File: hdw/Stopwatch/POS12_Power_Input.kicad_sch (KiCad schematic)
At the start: 17 parts

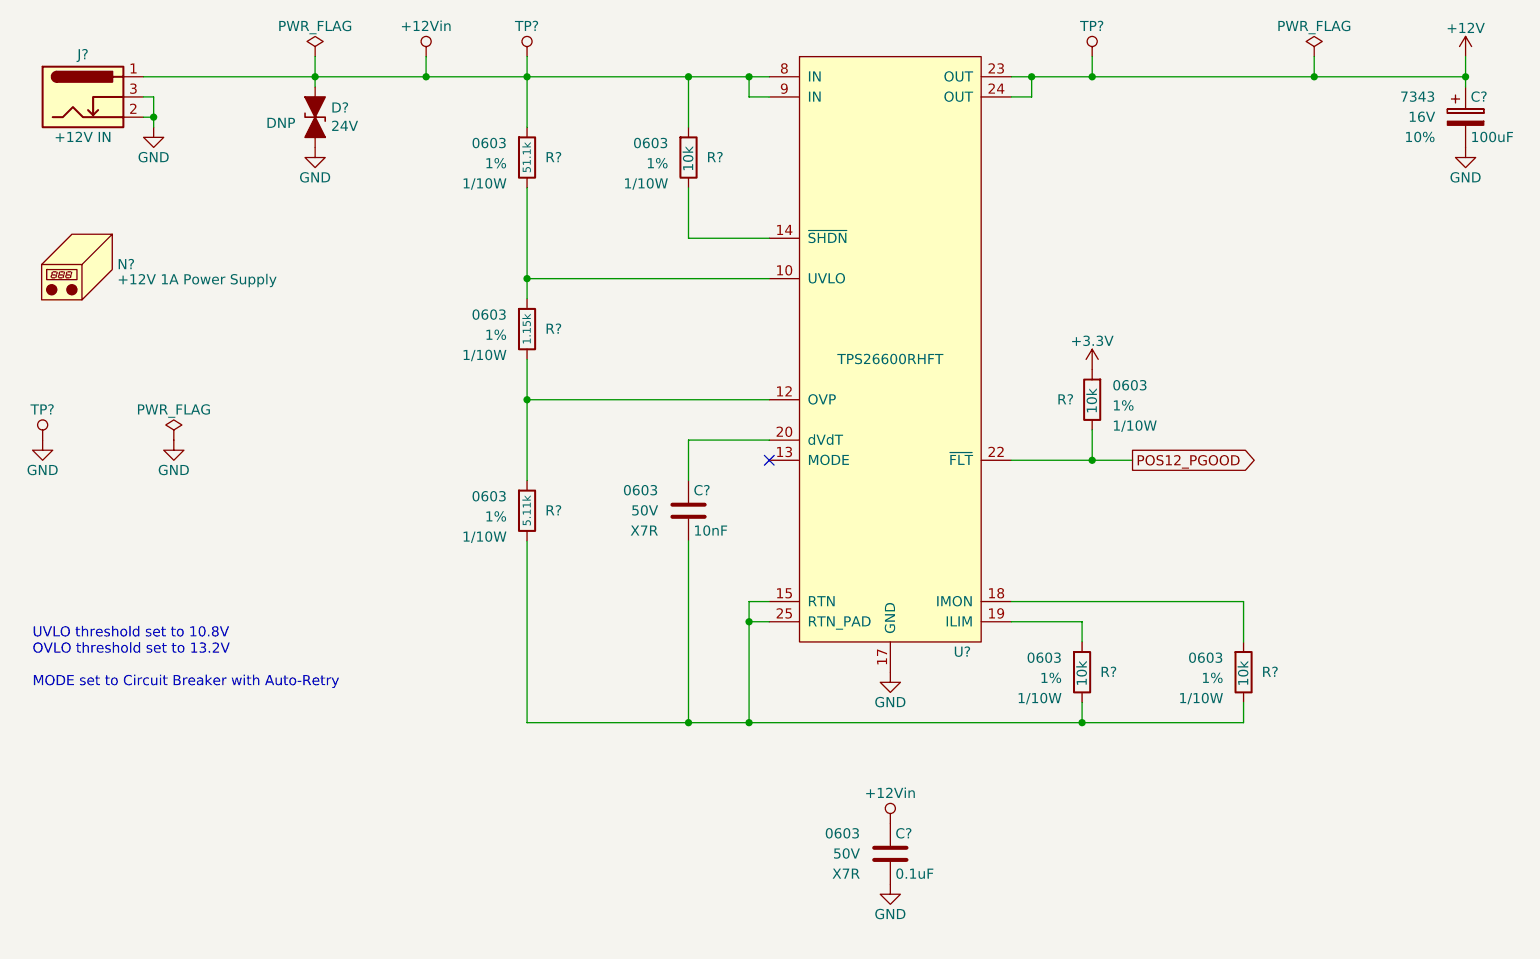
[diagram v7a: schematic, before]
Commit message: Assigned some digikey pns
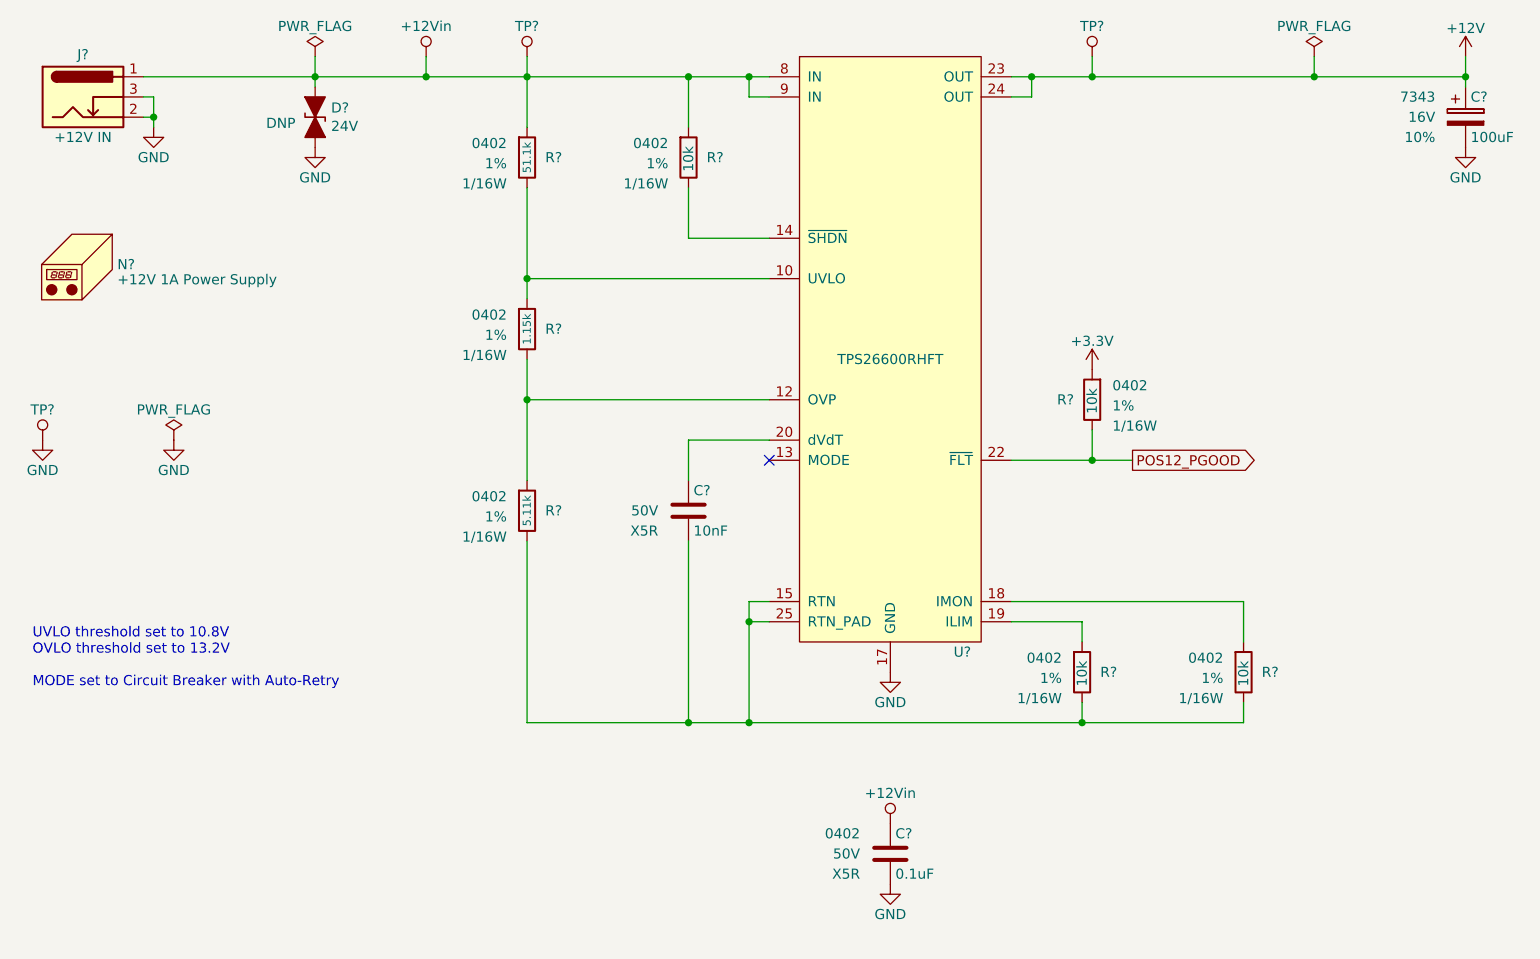
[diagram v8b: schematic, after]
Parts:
- C?: footprint Capacitors_SMD:C_0603 -> Capacitors_SMD:C_0402; Dielectric X7R -> X5R; Digi-Key PN 311-1344-1-ND -> 490-10697-1-ND; display_footprint 0603 -> 0402
- C?: footprint Capacitors_SMD:C_0603 -> Capacitors_SMD:C_0402; Dielectric X7R -> X5R; Digi-Key PN 1276-1921-1-ND -> 445-12201-1-ND; display_footprint 0603 -> (none)
- R? (x4): footprint Resistors_SMD:R_0603 -> Resistors_SMD:R_0402; Digi-Key PN RMCF0603FT10K0CT-ND -> RMCF0402FT10K0CT-ND; Wattage 1/10W -> 1/16W; display_footprint 0603 -> 0402
- R?: footprint Resistors_SMD:R_0603 -> Resistors_SMD:R_0402; Digi-Key PN RMCF0603FT10K0CT-ND -> RMCF0402FT1K15CT-ND; Wattage 1/10W -> 1/16W; display_footprint 0603 -> 0402
- R?: footprint Resistors_SMD:R_0603 -> Resistors_SMD:R_0402; Digi-Key PN RMCF0603FT10K0CT-ND -> RMCF0402FT51K1CT-ND; Wattage 1/10W -> 1/16W; display_footprint 0603 -> 0402
- R?: footprint Resistors_SMD:R_0603 -> Resistors_SMD:R_0402; Digi-Key PN RMCF0603FT10K0CT-ND -> RMCF0402FT5K11CT-ND; Wattage 1/10W -> 1/16W; display_footprint 0603 -> 0402
- TP?: Digi-Key PN 36-5005-ND -> (none)
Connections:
- net at U?.12 (OVP): now also R?.1, R?.2
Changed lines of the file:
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@@
       (effects (font (size 1.27 1.27)) (justify left))
     )
-    (property "Footprint" "Capacitors_SMD:C_0603" (at 143.2052 158.75 0)
+    (property "Footprint" "Capacitors_SMD:C_0402" (at 143.2052 158.75 0)
       (effects (font (size 1.27 1.27)) hide)
     )
@@
       (effects (font (size 1.27 1.27)) hide)
     )
-    (property "display_footprint" "0603" (at 138.43 152.4 0)
+    (property "display_footprint" "0402" (at 138.43 152.4 0)
       (effects (font (size 1.27 1.27)) (justify right))
     )
@@
       (effects (font (size 1.27 1.27)) (justify right))
     )
-    (property "Dielectric" "X7R" (at 138.43 157.48 0)
-      (effects (font (size 1.27 1.27)) (justify right))
-    )
-    (property "Digi-Key PN" "311-1344-1-ND" (at 153.035 142.24 0)
+    (property "Dielectric" "X5R" (at 138.43 157.48 0)
+      (effects (font (size 1.27 1.27)) (justify right))
+    )
+    (property "Digi-Key PN" "490-10697-1-ND" (at 153.035 142.24 0)
       (effects (font (size 1.524 1.524)) hide)
     )
@@
       (effects (font (size 1.27 1.27)) (justify left))
     )
-    (property "Footprint" "Resistors_SMD:R_0603" (at 167.64 97.79 0)
+    (property "Footprint" "Resistors_SMD:R_0402" (at 167.64 97.79 0)
       (effects (font (size 1.27 1.27)) hide)
     )
@@
       (effects (font (size 1.27 1.27)) hide)
     )
-    (property "display_footprint" "0603" (at 170.18 96.012 0)
+    (property "display_footprint" "0402" (at 170.18 96.012 0)
       (effects (font (size 1.27 1.27)) (justify left))
     )
@@
       (effects (font (size 1.27 1.27)) (justify left))
     )
-    (property "Wattage" "1/10W" (at 170.18 101.092 0)
-      (effects (font (size 1.27 1.27)) (justify left))
-    )
-    (property "Digi-Key PN" "RMCF0603FT10K0CT-ND" (at 175.26 87.63 0)
+    (property "Wattage" "1/16W" (at 170.18 101.092 0)
+      (effects (font (size 1.27 1.27)) (justify left))
+    )
+    (property "Digi-Key PN" "RMCF0402FT10K0CT-ND" (at 175.26 87.63 0)
       (effects (font (size 1.524 1.524)) hide)
     )
@@
       (effects (font (size 1.016 1.016)))
     )
-    (property "Footprint" "Resistors_SMD:R_0603" (at 96.52 88.9 0)
+    (property "Footprint" "Resistors_SMD:R_0402" (at 96.52 88.9 0)
       (effects (font (size 1.27 1.27)) hide)
     )
@@
       (effects (font (size 1.27 1.27)) hide)
     )
-    (property "display_footprint" "0603" (at 93.98 87.122 0)
+    (property "display_footprint" "0402" (at 93.98 87.122 0)
       (effects (font (size 1.27 1.27)) (justify left))
     )
@@
       (effects (font (size 1.27 1.27)) (justify left))
     )
-    (property "Wattage" "1/10W" (at 93.98 92.202 0)
-      (effects (font (size 1.27 1.27)) (justify left))
-    )
-    (property "Digi-Key PN" "RMCF0603FT10K0CT-ND" (at 88.9 78.74 0)
+    (property "Wattage" "1/16W" (at 93.98 92.202 0)
+      (effects (font (size 1.27 1.27)) (justify left))
+    )
+    (property "Digi-Key PN" "RMCF0402FT1K15CT-ND" (at 88.9 78.74 0)
       (effects (font (size 1.524 1.524)) hide)
     )
@@
       (effects (font (size 1.016 1.016)))
     )
-    (property "Footprint" "Resistors_SMD:R_0603" (at 96.52 67.31 0)
+    (property "Footprint" "Resistors_SMD:R_0402" (at 96.52 67.31 0)
       (effects (font (size 1.27 1.27)) hide)
     )
@@
       (effects (font (size 1.27 1.27)) hide)
     )
-    (property "display_footprint" "0603" (at 93.98 65.532 0)
+    (property "display_footprint" "0402" (at 93.98 65.532 0)
       (effects (font (size 1.27 1.27)) (justify left))
     )
@@
       (effects (font (size 1.27 1.27)) (justify left))
     )
-    (property "Wattage" "1/10W" (at 93.98 70.612 0)
-      (effects (font (size 1.27 1.27)) (justify left))
-    )
-    (property "Digi-Key PN" "RMCF0603FT10K0CT-ND" (at 88.9 57.15 0)
+    (property "Wattage" "1/16W" (at 93.98 70.612 0)
+      (effects (font (size 1.27 1.27)) (justify left))
+    )
+    (property "Digi-Key PN" "RMCF0402FT51K1CT-ND" (at 88.9 57.15 0)
       (effects (font (size 1.524 1.524)) hide)
     )
@@
       (effects (font (size 1.016 1.016)))
     )
-    (property "Footprint" "Resistors_SMD:R_0603" (at 96.52 111.76 0)
+    (property "Footprint" "Resistors_SMD:R_0402" (at 96.52 111.76 0)
       (effects (font (size 1.27 1.27)) hide)
     )
@@
       (effects (font (size 1.27 1.27)) hide)
     )
-    (property "display_footprint" "0603" (at 93.98 109.982 0)
+    (property "display_footprint" "0402" (at 93.98 109.982 0)
       (effects (font (size 1.27 1.27)) (justify left))
     )
@@
       (effects (font (size 1.27 1.27)) (justify left))
     )
-    (property "Wattage" "1/10W" (at 93.98 115.062 0)
-      (effects (font (size 1.27 1.27)) (justify left))
-    )
-    (property "Digi-Key PN" "RMCF0603FT10K0CT-ND" (at 88.9 101.6 0)
+    (property "Wattage" "1/16W" (at 93.98 115.062 0)
+      (effects (font (size 1.27 1.27)) (justify left))
+    )
+    (property "Digi-Key PN" "RMCF0402FT5K11CT-ND" (at 88.9 101.6 0)
       (effects (font (size 1.524 1.524)) hide)
     )
@@
       (effects (font (size 1.27 1.27)) (justify left))
     )
-    (property "Footprint" "Resistors_SMD:R_0603" (at 116.84 67.31 0)
+    (property "Footprint" "Resistors_SMD:R_0402" (at 116.84 67.31 0)
       (effects (font (size 1.27 1.27)) hide)
     )
@@
       (effects (font (size 1.27 1.27)) hide)
     )
-    (property "display_footprint" "0603" (at 114.3 65.532 0)
+    (property "display_footprint" "0402" (at 114.3 65.532 0)
       (effects (font (size 1.27 1.27)) (justify left))
     )
@@
       (effects (font (size 1.27 1.27)) (justify left))
     )
-    (property "Wattage" "1/10W" (at 114.3 70.612 0)
-      (effects (font (size 1.27 1.27)) (justify left))
-    )
-    (property "Digi-Key PN" "RMCF0603FT10K0CT-ND" (at 109.22 57.15 0)
+    (property "Wattage" "1/16W" (at 114.3 70.612 0)
+      (effects (font (size 1.27 1.27)) (justify left))
+    )
+    (property "Digi-Key PN" "RMCF0402FT10K0CT-ND" (at 109.22 57.15 0)
       (effects (font (size 1.524 1.524)) hide)
     )
@@
       (effects (font (size 1.524 1.524)))
     )
-    (property "Digi-Key PN" "36-5005-ND" (at 35.56 102.87 0)
+    (property "Digi-Key PN" "" (at 35.56 102.87 0)
       (effects (font (size 1.27 1.27)) hide)
     )
@@
       (effects (font (size 1.27 1.27)) (justify left))
     )
-    (property "Footprint" "Capacitors_SMD:C_0603" (at 117.8052 115.57 0)
+    (property "Footprint" "Capacitors_SMD:C_0402" (at 117.8052 115.57 0)
       (effects (font (size 1.27 1.27)) hide)
     )
@@
       (effects (font (size 1.27 1.27)) hide)
     )
-    (property "display_footprint" "0603" (at 113.03 109.22 0)
+    (property "display_footprint" "" (at 113.03 109.22 0)
       (effects (font (size 1.27 1.27)) (justify right))
     )
@@
       (effects (font (size 1.27 1.27)) (justify right))
     )
-    (property "Dielectric" "X7R" (at 113.03 114.3 0)
-      (effects (font (size 1.27 1.27)) (justify right))
-    )
-    (property "Digi-Key PN" "1276-1921-1-ND" (at 127.635 99.06 0)
+    (property "Dielectric" "X5R" (at 113.03 114.3 0)
+      (effects (font (size 1.27 1.27)) (justify right))
+    )
+    (property "Digi-Key PN" "445-12201-1-ND" (at 127.635 99.06 0)
       (effects (font (size 1.524 1.524)) hide)
     )
@@
       (effects (font (size 1.27 1.27)) (justify left))
     )
-    (property "Footprint" "Resistors_SMD:R_0603" (at 186.69 132.08 0)
+    (property "Footprint" "Resistors_SMD:R_0402" (at 186.69 132.08 0)
       (effects (font (size 1.27 1.27)) hide)
     )
@@
       (effects (font (size 1.27 1.27)) hide)
     )
-    (property "display_footprint" "0603" (at 184.15 130.302 0)
+    (property "display_footprint" "0402" (at 184.15 130.302 0)
       (effects (font (size 1.27 1.27)) (justify left))
     )
@@
       (effects (font (size 1.27 1.27)) (justify left))
     )
-    (property "Wattage" "1/10W" (at 184.15 135.382 0)
-      (effects (font (size 1.27 1.27)) (justify left))
-    )
-    (property "Digi-Key PN" "RMCF0603FT10K0CT-ND" (at 179.07 121.92 0)
+    (property "Wattage" "1/16W" (at 184.15 135.382 0)
+      (effects (font (size 1.27 1.27)) (justify left))
+    )
+    (property "Digi-Key PN" "RMCF0402FT10K0CT-ND" (at 179.07 121.92 0)
       (effects (font (size 1.524 1.524)) hide)
     )
@@
       (effects (font (size 1.27 1.27)) (justify left))
     )
-    (property "Footprint" "Resistors_SMD:R_0603" (at 166.37 132.08 0)
+    (property "Footprint" "Resistors_SMD:R_0402" (at 166.37 132.08 0)
       (effects (font (size 1.27 1.27)) hide)
     )
@@
       (effects (font (size 1.27 1.27)) hide)
     )
-    (property "display_footprint" "0603" (at 163.83 130.302 0)
+    (property "display_footprint" "0402" (at 163.83 130.302 0)
       (effects (font (size 1.27 1.27)) (justify left))
     )
@@
       (effects (font (size 1.27 1.27)) (justify left))
     )
-    (property "Wattage" "1/10W" (at 163.83 135.382 0)
-      (effects (font (size 1.27 1.27)) (justify left))
-    )
-    (property "Digi-Key PN" "RMCF0603FT10K0CT-ND" (at 158.75 121.92 0)
-      (effects (font (size 1.524 1.524)) hide)
-    )
+    (property "Wattage" "1/16W" (at 163.83 135.382 0)
+      (effects (font (size 1.27 1.27)) (justify left))
+    )
+    (property "Digi-Key PN" "RMCF0402FT10K0CT-ND" (at 158.75 121.92 0)
+      (effects (font (size 1.524 1.524)) hide)
+    )
